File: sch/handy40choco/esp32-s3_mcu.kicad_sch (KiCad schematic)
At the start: 44 parts, among them J3 USB_C_Receptacle_USB2.0_16P, J4 Conn_01x04, SW41 SW_Push, SW42 SW_Push, U3 ESP32-S3-WROOM-1, U4 MIC5219-3.3YM5, Y1 32k

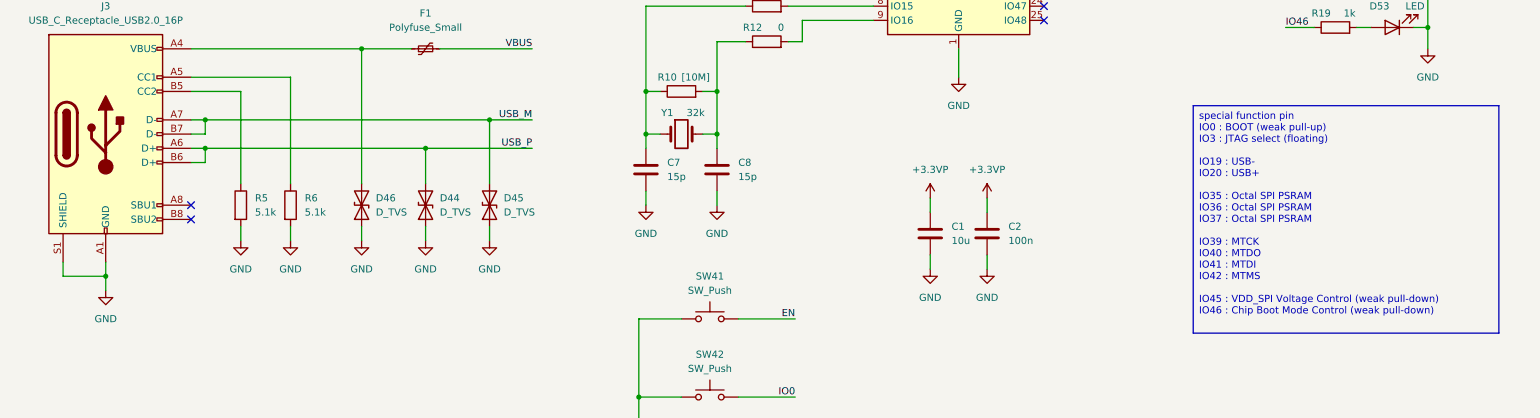
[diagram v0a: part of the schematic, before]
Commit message: Kicad 9に変更しました。 マイコン基板から16ピンのピンヘッダに変更しました。
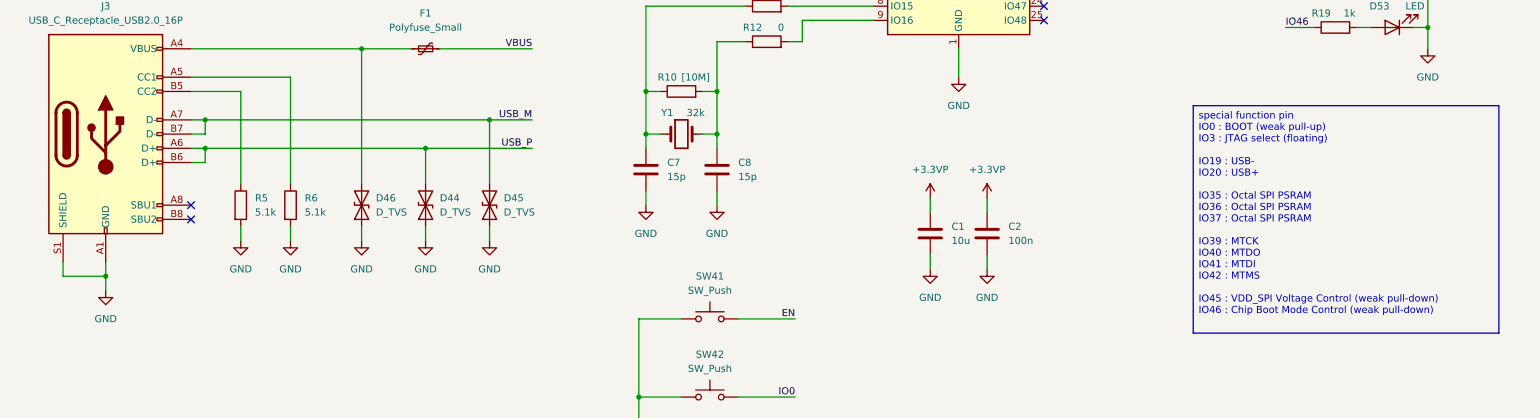
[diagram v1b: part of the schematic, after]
